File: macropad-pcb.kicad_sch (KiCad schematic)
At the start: 11 parts

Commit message: rev2 ready for sleeping on
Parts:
- added J1, J10, J2, J3, J4, J5, J6, J7, J8, J9: Conn_01x01_Socket, Connector_PinHeader_2.54mm:PinHeader_1x01_P2.54mm_Vertical, symbol Connector:Conn_01x01_Socket
- added LOGO1: **REF, ct-kicad:awesome-logo, symbol ct-kicad:awesome-logo
- added LOGO2: **REF, ct-kicad:qmk-lite, symbol ct-kicad:qmk-lite-logo
- H1, H2: footprint MountingHole:MountingHole_3mm -> MountingHole:MountingHole_3mm_Pad_Via
- renumbered MAIN to MAIN1
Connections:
- net GND: now also MAIN1.17, MAIN1.18, R8C10.14, R8C10.15, R8C10.4, R8C10.5, R8C11.14, R8C11.15, R8C11.4, R8C11.5, R8C8.14, R8C8.15, R8C8.4, R8C8.5, R8C9.14, R8C9.15, R8C9.4, R8C9.5, R9C10.14, R9C10.15, R9C10.4, R9C10.5, R9C11.14, R9C11.15, R9C11.4, R9C11.5, R9C8.14, R9C8.15, R9C8.4, R9C8.5, R9C9.14, R9C9.15, R9C9.4, R9C9.5, J10.1 (Pin_1); no longer R8C10.10, R8C10.9, R8C11.10, R8C11.9, R8C8.10, R8C8.9, R8C9.10, R8C9.9, R9C10.10, R9C10.9, R9C11.10, R9C11.9, R9C8.10, R9C8.9, R9C9.10, R9C9.9
- net LED_DO_MACRO: now also R9C11.3, J5.1 (Pin_1); no longer R9C11.11
- net VCC: now also R8C10.10, R8C10.11, R8C10.12, R8C10.9, R8C11.10, R8C11.11, R8C11.12, R8C11.9, R8C8.10, R8C8.11, R8C8.12, R8C8.9, R8C9.10, R8C9.11, R8C9.12, R8C9.9, R9C10.10, R9C10.11, R9C10.12, R9C10.9, R9C11.10, R9C11.11, R9C11.12, R9C11.9, R9C8.10, R9C8.11, R9C8.12, R9C8.9, R9C9.10, R9C9.11, R9C9.12, R9C9.9, J9.1 (Pin_1); no longer R8C10.2, R8C10.3, R8C10.4, R8C10.5, R8C11.2, R8C11.3, R8C11.4, R8C11.5, R8C8.2, R8C8.3, R8C8.4, R8C8.5, R8C9.2, R8C9.3, R8C9.4, R8C9.5, R9C10.2, R9C10.3, R9C10.4, R9C10.5, R9C11.2, R9C11.3, R9C11.4, R9C11.5, R9C8.2, R9C8.3, R9C8.4, R9C8.5, R9C9.2, R9C9.3, R9C9.4, R9C9.5
- net col10: now also R8C10.2, R9C10.2, J3.1 (Pin_1); no longer R8C10.12, R9C10.12
- net col11: now also R8C11.2, R9C11.2, J4.1 (Pin_1); no longer R8C11.12, R9C11.12
- net col8: now also R8C8.2, R9C8.2, J1.1 (Pin_1); no longer R8C8.12, R9C8.12
- net col9: now also R8C9.2, R9C9.2, J2.1 (Pin_1); no longer R8C9.12, R9C9.12
- net from_row_9_DO: now also R8C11.3, R9C8.13; no longer R8C11.11, R9C8.1
- net row8: now also R8C10.1, R8C11.1, R8C8.1, R8C9.1, J6.1 (Pin_1); no longer R8C10.13, R8C11.13, R8C8.13, R8C9.13
- net row9: now also R9C10.1, R9C11.1, R9C8.1, R9C9.1, J7.1 (Pin_1); no longer R9C10.13, R9C11.13, R9C8.13, R9C9.13
- net LED_DI: now reaches MAIN1.11
- net LED_DI: now also R8C8.13, J8.1 (Pin_1); no longer R8C8.1
- new net: R9C10.3, R9C11.13
- new net: R8C10.3, R8C11.13
- new net: R9C8.3, R9C9.13
- new net: R9C10.13, R9C9.3
- new net: R8C8.3, R8C9.13
- new net: R8C10.13, R8C9.3
- no-connect marks 16 -> 0

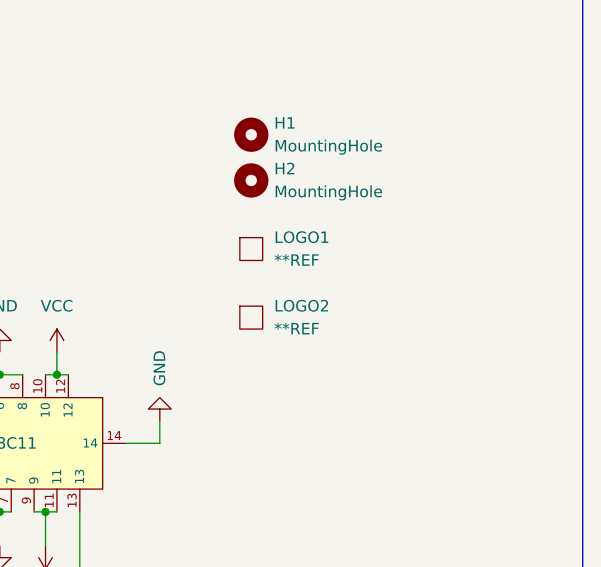
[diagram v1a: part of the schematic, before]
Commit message: more updates to the board, waiting on cyboard logo
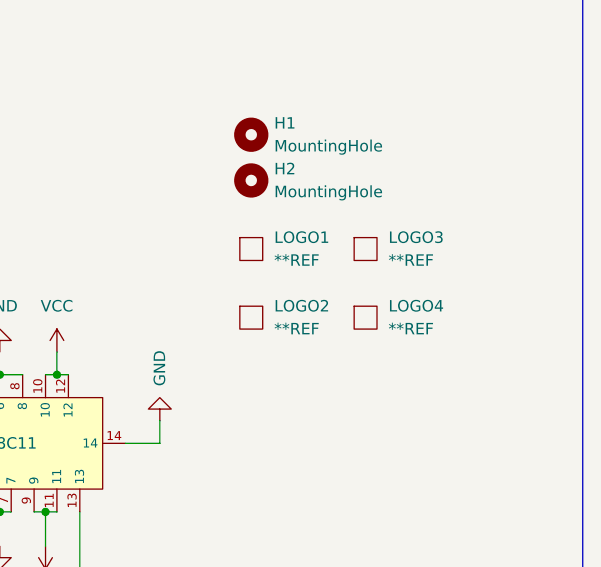
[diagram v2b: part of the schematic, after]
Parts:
- added LOGO3: **REF, ct-kicad:awesome-logo, symbol ct-kicad:awesome-logo
- added LOGO4: **REF, ct-kicad:macropad-pcb-qr-10mm, symbol ct-kicad:macropad-qr-15mm
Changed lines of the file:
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@@
+    )
+  )
+  (symbol (lib_id "ct-kicad:macropad-qr-15mm") (at 252.73 66.04 0) (unit 1)
+    (in_bom no) (on_board yes) (dnp no) (fields_autoplaced)
+    (property "Reference" "LOGO4" (at 255.27 64.77 0)
+      (effects (font (size 1.27 1.27)) (justify left))
+    )
+    (property "Value" "**REF" (at 255.27 67.31 0)
+      (effects (font (size 1.27 1.27)) (justify left))
+    )
+    (property "Footprint" "ct-kicad:macropad-pcb-qr-10mm" (at 252.73 66.04 0)
+      (effects (font (size 1.27 1.27)) hide)
+    )
+    (property "Datasheet" "" (at 252.73 66.04 0)
+      (effects (font (size 1.27 1.27)) hide)
+    )
+    (instances
+      (project "macropad-pcb"
+        (path "/a1d63ebf-3d6e-4f37-a8f0-07094ad9e2ad"
+          (reference "LOGO4") (unit 1)
+        )
+      )
     )
   )
@@
         )
       )
+    )
+  )
+  (symbol (lib_id "ct-kicad:awesome-logo") (at 252.73 58.42 0) (unit 1)
+    (in_bom no) (on_board yes) (dnp no) (fields_autoplaced)
+    (property "Reference" "LOGO3" (at 255.27 57.15 0)
+      (effects (font (size 1.27 1.27)) (justify left))
+    )
+    (property "Value" "**REF" (at 255.27 59.69 0)
+      (effects (font (size 1.27 1.27)) (justify left))
+    )
+    (property "Footprint" "ct-kicad:awesome-logo" (at 252.73 58.42 0)
+      (effects (font (size 1.27 1.27)) hide)
+    )
+    (property "Datasheet" "" (at 252.73 58.42 0)
+      (effects (font (size 1.27 1.27)) hide)
+    )
+    (instances
+      (project "macropad-pcb"
+        (path "/a1d63ebf-3d6e-4f37-a8f0-07094ad9e2ad"
+          (reference "LOGO3") (unit 1)
+        )
+      )
